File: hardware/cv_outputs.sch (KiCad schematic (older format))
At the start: 17 parts

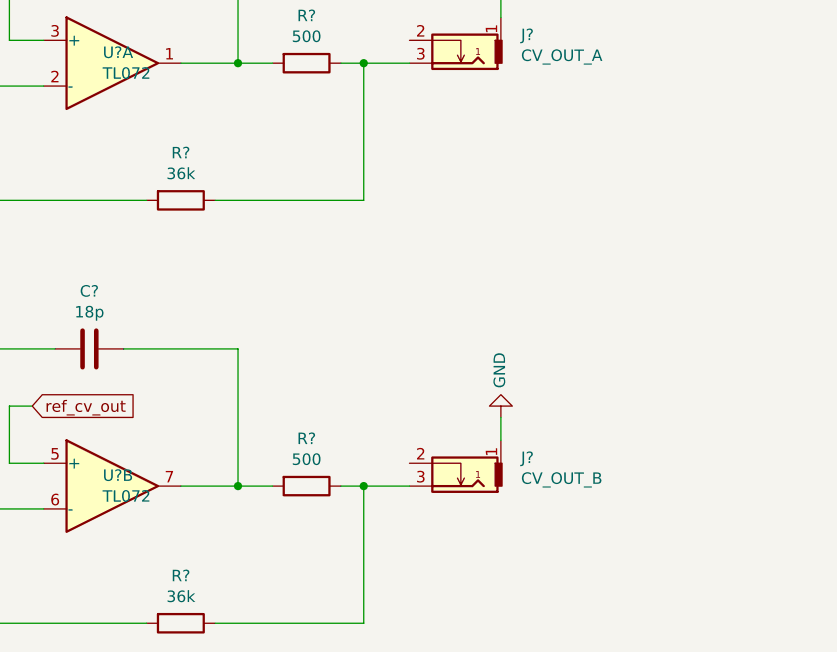
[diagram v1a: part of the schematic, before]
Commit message: Adjust CV-ins
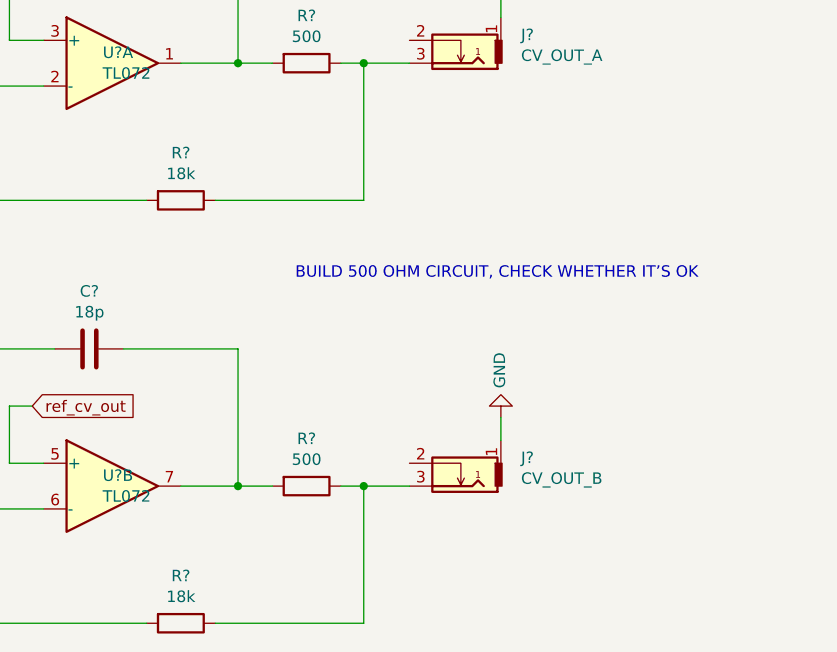
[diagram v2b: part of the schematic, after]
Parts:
- R? (x2): value 36k -> 18k
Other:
- note added: "BUILD 500 OHM CIRCUIT, CHECK WHETHER IT’S OK"
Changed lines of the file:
@@
 P 6900 3450
 F 0 "R?" V 6693 3450 50  0000 C CNN
-F 1 "36k" V 6784 3450 50  0000 C CNN
+F 1 "18k" V 6784 3450 50  0000 C CNN
 F 2 "" V 6830 3450 50  0001 C CNN
 F 3 "~" H 6900 3450 50  0001 C CNN
@@
 P 6900 5300
 F 0 "R?" V 6693 5300 50  0000 C CNN
-F 1 "36k" V 6784 5300 50  0000 C CNN
+F 1 "18k" V 6784 5300 50  0000 C CNN
 F 2 "" V 6830 5300 50  0001 C CNN
 F 3 "~" H 6900 5300 50  0001 C CNN
@@
 Wire Wire Line
 	7700 4700 7900 4700
+Text Notes 7400 3800 0    50   ~ 0
+BUILD 500 OHM CIRCUIT, CHECK WHETHER IT’S OK
 $EndSCHEMATC

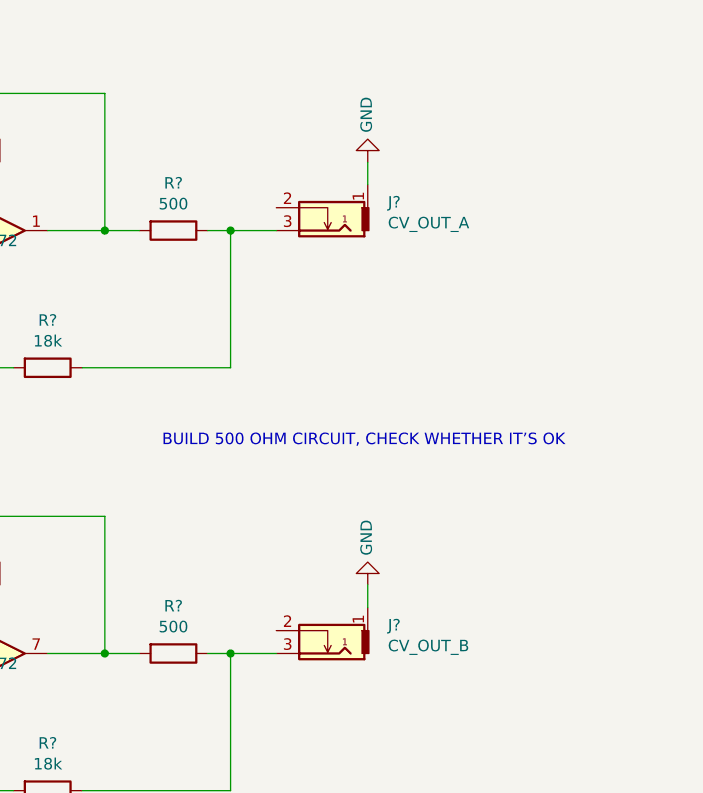
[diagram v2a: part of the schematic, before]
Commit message: Add more schematics:
- Faders
- Step LEDs
- Trigger output
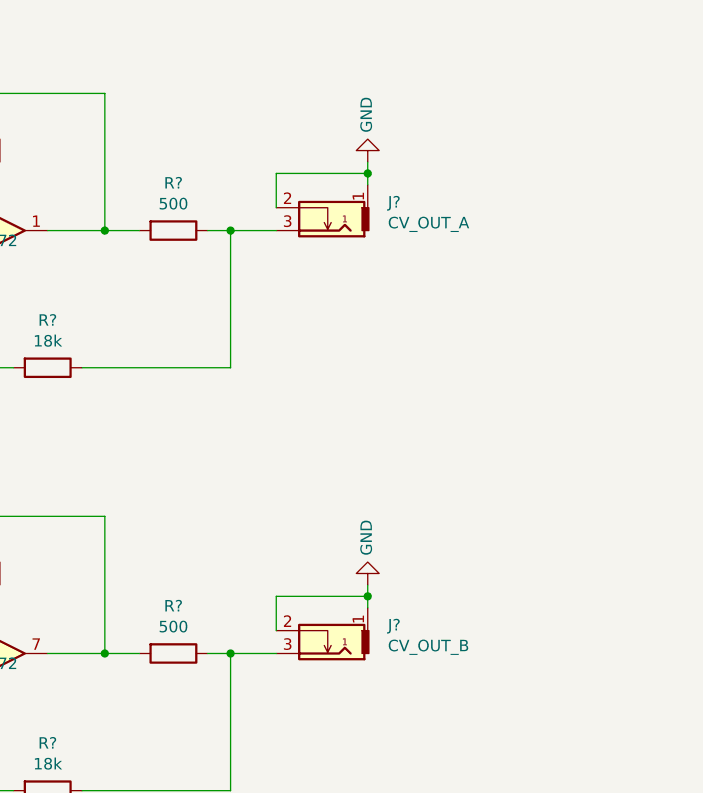
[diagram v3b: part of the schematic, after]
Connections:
- net GND: now also J?.2, J?.2
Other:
- note removed: "BUILD 500 OHM CIRCUIT, CHECK WHETHER IT’S OK"
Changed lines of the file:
@@
 $Descr A4 11693 8268
 encoding utf-8
-Sheet 4 6
+Sheet 4 9
 Title ""
 Date ""
@@
 $EndComp
 $Comp
-L power:GND #PWR?
+L power:GND #PWR0110
 U 1 1 5FB847AF
 P 1450 2000
-F 0 "#PWR?" H 1450 1750 50  0001 C CNN
+F 0 "#PWR0110" H 1450 1750 50  0001 C CNN
 F 1 "GND" V 1455 1872 50  0000 R CNN
 F 2 "" H 1450 2000 50  0001 C CNN
@@
 $EndComp
 $Comp
-L power:VEE #PWR?
+L power:VEE #PWR0111
 U 1 1 5FB9194E
 P 2650 2000
-F 0 "#PWR?" H 2650 1850 50  0001 C CNN
+F 0 "#PWR0111" H 2650 1850 50  0001 C CNN
 F 1 "VEE" H 2665 2173 50  0000 C CNN
 F 2 "" H 2650 2000 50  0001 C CNN
@@
 $EndComp
 $Comp
-L power:VCC #PWR?
+L power:VCC #PWR0112
 U 1 1 5FB924D1
 P 2650 1400
-F 0 "#PWR?" H 2650 1250 50  0001 C CNN
+F 0 "#PWR0112" H 2650 1250 50  0001 C CNN
 F 1 "VCC" H 2665 1573 50  0000 C CNN
 F 2 "" H 2650 1400 50  0001 C CNN
@@
 $EndComp
 $Comp
-L power:VCC #PWR?
+L power:VCC #PWR0113
 U 1 1 5FB9836B
 P 3650 1450
-F 0 "#PWR?" H 3650 1300 50  0001 C CNN
+F 0 "#PWR0113" H 3650 1300 50  0001 C CNN
 F 1 "VCC" H 3665 1623 50  0000 C CNN
 F 2 "" H 3650 1450 50  0001 C CNN
@@
 $EndComp
 $Comp
-L power:VEE #PWR?
+L power:VEE #PWR0114
 U 1 1 5FB98880
 P 4250 1450
-F 0 "#PWR?" H 4250 1300 50  0001 C CNN
+F 0 "#PWR0114" H 4250 1300 50  0001 C CNN
 F 1 "VEE" H 4265 1623 50  0000 C CNN
 F 2 "" H 4250 1450 50  0001 C CNN
@@
 $EndComp
 $Comp
-L power:GND #PWR?
+L power:GND #PWR0115
 U 1 1 5FB99275
 P 3950 1950
-F 0 "#PWR?" H 3950 1700 50  0001 C CNN
+F 0 "#PWR0115" H 3950 1700 50  0001 C CNN
 F 1 "GND" V 3955 1822 50  0000 R CNN
 F 2 "" H 3950 1950 50  0001 C CNN
@@
 $EndComp
 $Comp
-L power:GND #PWR?
+L power:GND #PWR0116
 U 1 1 5FBBFB43
 P 8300 2550
-F 0 "#PWR?" H 8300 2300 50  0001 C CNN
+F 0 "#PWR0116" H 8300 2300 50  0001 C CNN
 F 1 "GND" V 8305 2422 50  0000 R CNN
 F 2 "" H 8300 2550 50  0001 C CNN
@@
 $EndComp
 Wire Wire Line
-	8300 2550 8300 2650
+	8300 2550 8300 2600
 $Comp
 L thonkiconn_jackSocket_fuzzySi:fuzzySI_thonkiconn J?
@@
 $EndComp
 $Comp
-L power:GND #PWR?
+L power:GND #PWR0117
 U 1 1 5FBC5571
 P 8300 4400
-F 0 "#PWR?" H 8300 4150 50  0001 C CNN
+F 0 "#PWR0117" H 8300 4150 50  0001 C CNN
 F 1 "GND" V 8305 4272 50  0000 R CNN
 F 2 "" H 8300 4400 50  0001 C CNN
@@
 $EndComp
 Wire Wire Line
-	8300 4400 8300 4500
+	8300 4400 8300 4450
 Wire Wire Line
 	7700 2850 7900 2850
@@
 Wire Wire Line
 	7700 4700 7900 4700
-Text Notes 7400 3800 0    50   ~ 0
-BUILD 500 OHM CIRCUIT, CHECK WHETHER IT’S OK
+Wire Wire Line
+	7900 2750 7900 2600
+Wire Wire Line
+	7900 2600 8300 2600
+Connection ~ 8300 2600
+Wire Wire Line
+	8300 2600 8300 2650
+Wire Wire Line
+	7900 4600 7900 4450
+Wire Wire Line
+	7900 4450 8300 4450
+Connection ~ 8300 4450
+Wire Wire Line
+	8300 4450 8300 4500
 $EndSCHEMATC

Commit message: Minor adjustments to schematics before PCB
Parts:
- removed J?: CV_OUT_A, symbol thonkiconn_jackSocket_fuzzySi:fuzzySI_thonkiconn
- removed J?: CV_OUT_B, symbol thonkiconn_jackSocket_fuzzySi:fuzzySI_thonkiconn
- added J5, J6: PJ398SM, Connector_Audio:Jack_3.5mm_QingPu_WQP-PJ398SM_Vertical_CircularHoles, symbol Connector:AudioJack2_SwitchT
- C16, C17: renamed from C?; footprint (none) -> Capacitor_SMD:C_0603_1608Metric
- C18, C19: renamed from C?; value 18p -> 7p; footprint (none) -> Capacitor_SMD:C_0603_1608Metric
- R10, R11: renamed from R?; value 18k -> 270k; footprint (none) -> Resistor_SMD:R_0603_1608Metric
- R12, R13, R6, R7: renamed from R?; footprint (none) -> Resistor_SMD:R_0603_1608Metric
- R8, R9: renamed from R?; value 10k -> 75k; footprint (none) -> Resistor_SMD:R_0603_1608Metric
- U2: renamed from U?; footprint (none) -> Package_SO:SOIC-8_3.9x4.9mm_P1.27mm
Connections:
- net GND: now also J5.S, J5.TN, J6.S, J6.TN
- net at R11.1, R13.1: now also J6.T
- net at R10.1, R12.1: now also J5.T

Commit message: Last adjustments to hardware before v0.1 release
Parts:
- C17: renamed from C16; LCSC (none) -> C14663; LCSC Part # (none) -> C14663
- C18: renamed from C17; LCSC (none) -> C14663; LCSC Part # (none) -> C14663
- C19: renamed from C18; value 7p -> 10p; LCSC (none) -> C1634; LCSC Part # (none) -> C1634
- C20: renamed from C19; value 7p -> 10p; LCSC (none) -> C1634; LCSC Part # (none) -> C1634
- R12, R13: value 500 -> 470R; LCSC (none) -> C23179; LCSC Part # (none) -> C23179
- U2: LCSC (none) -> C6961; LCSC Part # (none) -> C6961
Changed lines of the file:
@@
 $EndComp
 $Comp
-L power:GND #PWR035
+L power:GND #PWR041
 U 1 1 5FB847AF
 P 1450 2000
-F 0 "#PWR035" H 1450 1750 50  0001 C CNN
+F 0 "#PWR041" H 1450 1750 50  0001 C CNN
 F 1 "GND" V 1455 1872 50  0000 R CNN
 F 2 "" H 1450 2000 50  0001 C CNN
@@
 F 6 "Y" H 6600 2850 50  0001 C CNN "Spice_Netlist_Enabled"
 F 7 "tl072-dual.cir" H 6600 2850 50  0001 C CNN "Spice_Lib_File"
+F 8 "C6961" H 6600 2850 50  0001 C CNN "LCSC Part #"
+F 9 "C6961" H 6600 2850 50  0001 C CNN "LCSC"
 	1    6600 2850
 	1    0    0    -1
 $EndComp
 $Comp
-L Device:C C18
+L Device:C C19
 U 1 1 5FB847D0
 P 6500 2250
-F 0 "C18" V 6248 2250 50  0000 C CNN
-F 1 "7p" V 6339 2250 50  0000 C CNN
+F 0 "C19" V 6248 2250 50  0000 C CNN
+F 1 "10p" V 6339 2250 50  0000 C CNN
 F 2 "Capacitor_SMD:C_0603_1608Metric" H 6538 2100 50  0001 C CNN
 F 3 "~" H 6500 2250 50  0001 C CNN
+F 4 "C1634" H 6500 2250 50  0001 C CNN "LCSC Part #"
+F 5 "C1634" H 6500 2250 50  0001 C CNN "LCSC"
 	1    6500 2250
 	0    1    1    0
@@
 P 7450 2850
 F 0 "R12" V 7243 2850 50  0000 C CNN
-F 1 "500" V 7334 2850 50  0000 C CNN
+F 1 "470R" V 7334 2850 50  0000 C CNN
 F 2 "Resistor_SMD:R_0603_1608Metric" V 7380 2850 50  0001 C CNN
 F 3 "~" H 7450 2850 50  0001 C CNN
+F 4 "C23179" H 7450 2850 50  0001 C CNN "LCSC Part #"
+F 5 "C23179" H 7450 2850 50  0001 C CNN "LCSC"
 	1    7450 2850
 	0    1    1    0
@@
 F 6 "Y" H 2750 1700 50  0001 C CNN "Spice_Netlist_Enabled"
 F 7 "tl072-dual.cir" H 2750 1700 50  0001 C CNN "Spice_Lib_File"
+F 8 "C6961" H 2750 1700 50  0001 C CNN "LCSC Part #"
+F 9 "C6961" H 2750 1700 50  0001 C CNN "LCSC"
 	3    2750 1700
 	1    0    0    -1
 $EndComp
 $Comp
-L power:VEE #PWR037
+L power:VEE #PWR043
 U 1 1 5FB9194E
 P 2650 2000
-F 0 "#PWR037" H 2650 1850 50  0001 C CNN
+F 0 "#PWR043" H 2650 1850 50  0001 C CNN
 F 1 "VEE" H 2665 2173 50  0000 C CNN
 F 2 "" H 2650 2000 50  0001 C CNN
@@
 $EndComp
 $Comp
-L power:VCC #PWR036
+L power:VCC #PWR042
 U 1 1 5FB924D1
 P 2650 1400
-F 0 "#PWR036" H 2650 1250 50  0001 C CNN
+F 0 "#PWR042" H 2650 1250 50  0001 C CNN
 F 1 "VCC" H 2665 1573 50  0000 C CNN
 F 2 "" H 2650 1400 50  0001 C CNN
@@
 F 6 "Y" H 6600 4700 50  0001 C CNN "Spice_Netlist_Enabled"
 F 7 "tl072-dual.cir" H 6600 4700 50  0001 C CNN "Spice_Lib_File"
+F 8 "C6961" H 6600 4700 50  0001 C CNN "LCSC Part #"
+F 9 "C6961" H 6600 4700 50  0001 C CNN "LCSC"
 	2    6600 4700
 	1    0    0    -1
 $EndComp
 $Comp
-L Device:C C19
+L Device:C C20
 U 1 1 5FB82D0C
 P 6500 4100
-F 0 "C19" V 6248 4100 50  0000 C CNN
-F 1 "7p" V 6339 4100 50  0000 C CNN
+F 0 "C20" V 6248 4100 50  0000 C CNN
+F 1 "10p" V 6339 4100 50  0000 C CNN
 F 2 "Capacitor_SMD:C_0603_1608Metric" H 6538 3950 50  0001 C CNN
 F 3 "~" H 6500 4100 50  0001 C CNN
+F 4 "C1634" H 6500 4100 50  0001 C CNN "LCSC Part #"
+F 5 "C1634" H 6500 4100 50  0001 C CNN "LCSC"
 	1    6500 4100
 	0    1    1    0
@@
 P 7450 4700
 F 0 "R13" V 7243 4700 50  0000 C CNN
-F 1 "500" V 7334 4700 50  0000 C CNN
+F 1 "470R" V 7334 4700 50  0000 C CNN
 F 2 "Resistor_SMD:R_0603_1608Metric" V 7380 4700 50  0001 C CNN
 F 3 "~" H 7450 4700 50  0001 C CNN
+F 4 "C23179" H 7450 4700 50  0001 C CNN "LCSC Part #"
+F 5 "C23179" H 7450 4700 50  0001 C CNN "LCSC"
 	1    7450 4700
 	0    1    1    0
@@
 dac_channel_b
 $Comp
-L Device:C C16
+L Device:C C17
 U 1 1 5FB976CE
 P 3650 1600
-F 0 "C16" V 3398 1600 50  0000 C CNN
+F 0 "C17" V 3398 1600 50  0000 C CNN
 F 1 "100n" V 3489 1600 50  0000 C CNN
 F 2 "Capacitor_SMD:C_0603_1608Metric" H 3688 1450 50  0001 C CNN
 F 3 "~" H 3650 1600 50  0001 C CNN
+F 4 "C14663" H 3650 1600 50  0001 C CNN "LCSC Part #"
+F 5 "C14663" H 3650 1600 50  0001 C CNN "LCSC"
 	1    3650 1600
 	-1   0    0    1
 $EndComp
 $Comp
-L Device:C C17
+L Device:C C18
 U 1 1 5FB97D49
 P 4250 1600
-F 0 "C17" V 3998 1600 50  0000 C CNN
+F 0 "C18" V 3998 1600 50  0000 C CNN
 F 1 "100n" V 4089 1600 50  0000 C CNN
 F 2 "Capacitor_SMD:C_0603_1608Metric" H 4288 1450 50  0001 C CNN
 F 3 "~" H 4250 1600 50  0001 C CNN
+F 4 "C14663" H 4250 1600 50  0001 C CNN "LCSC Part #"
+F 5 "C14663" H 4250 1600 50  0001 C CNN "LCSC"
 	1    4250 1600
 	-1   0    0    1
 $EndComp
 $Comp
-L power:VCC #PWR038
+L power:VCC #PWR044
 U 1 1 5FB9836B
 P 3650 1450
-F 0 "#PWR038" H 3650 1300 50  0001 C CNN
+F 0 "#PWR044" H 3650 1300 50  0001 C CNN
 F 1 "VCC" H 3665 1623 50  0000 C CNN
 F 2 "" H 3650 1450 50  0001 C CNN
@@
 $EndComp
 $Comp
-L power:VEE #PWR040
+L power:VEE #PWR046
 U 1 1 5FB98880
 P 4250 1450
-F 0 "#PWR040" H 4250 1300 50  0001 C CNN
+F 0 "#PWR046" H 4250 1300 50  0001 C CNN
 F 1 "VEE" H 4265 1623 50  0000 C CNN
 F 2 "" H 4250 1450 50  0001 C CNN
@@
 $EndComp
 $Comp
-L power:GND #PWR039
+L power:GND #PWR045
 U 1 1 5FB99275
 P 3950 1950
-F 0 "#PWR039" H 3950 1700 50  0001 C CNN
+F 0 "#PWR045" H 3950 1700 50  0001 C CNN
 F 1 "GND" V 3955 1822 50  0000 R CNN
 F 2 "" H 3950 1950 50  0001 C CNN
@@
 	8100 2950 8100 3000
 $Comp
-L power:GND #PWR041
+L power:GND #PWR047
 U 1 1 5FBBFB43
 P 8100 3100
-F 0 "#PWR041" H 8100 2850 50  0001 C CNN
+F 0 "#PWR047" H 8100 2850 50  0001 C CNN
 F 1 "GND" V 8105 2972 50  0000 R CNN
 F 2 "" H 8100 3100 50  0001 C CNN
@@
 	8100 4800 8100 4850
 $Comp
-L power:GND #PWR042
+L power:GND #PWR048
 U 1 1 5FEFC60D
 P 8100 4950
-F 0 "#PWR042" H 8100 4700 50  0001 C CNN
+F 0 "#PWR048" H 8100 4700 50  0001 C CNN
 F 1 "GND" V 8105 4822 50  0000 R CNN
 F 2 "" H 8100 4950 50  0001 C CNN

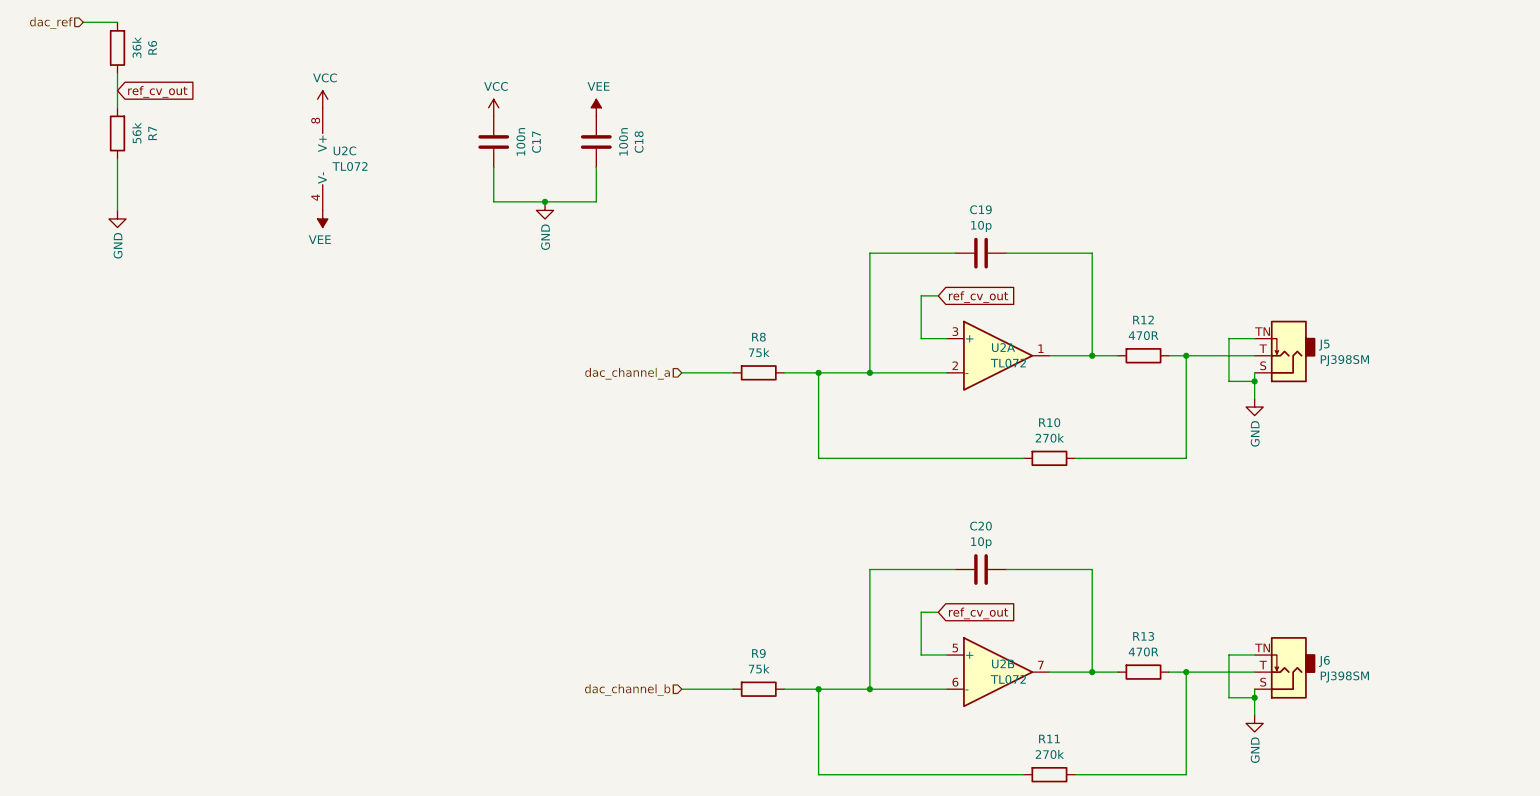
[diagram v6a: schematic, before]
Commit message: Re-adjust resistor values for CV-out
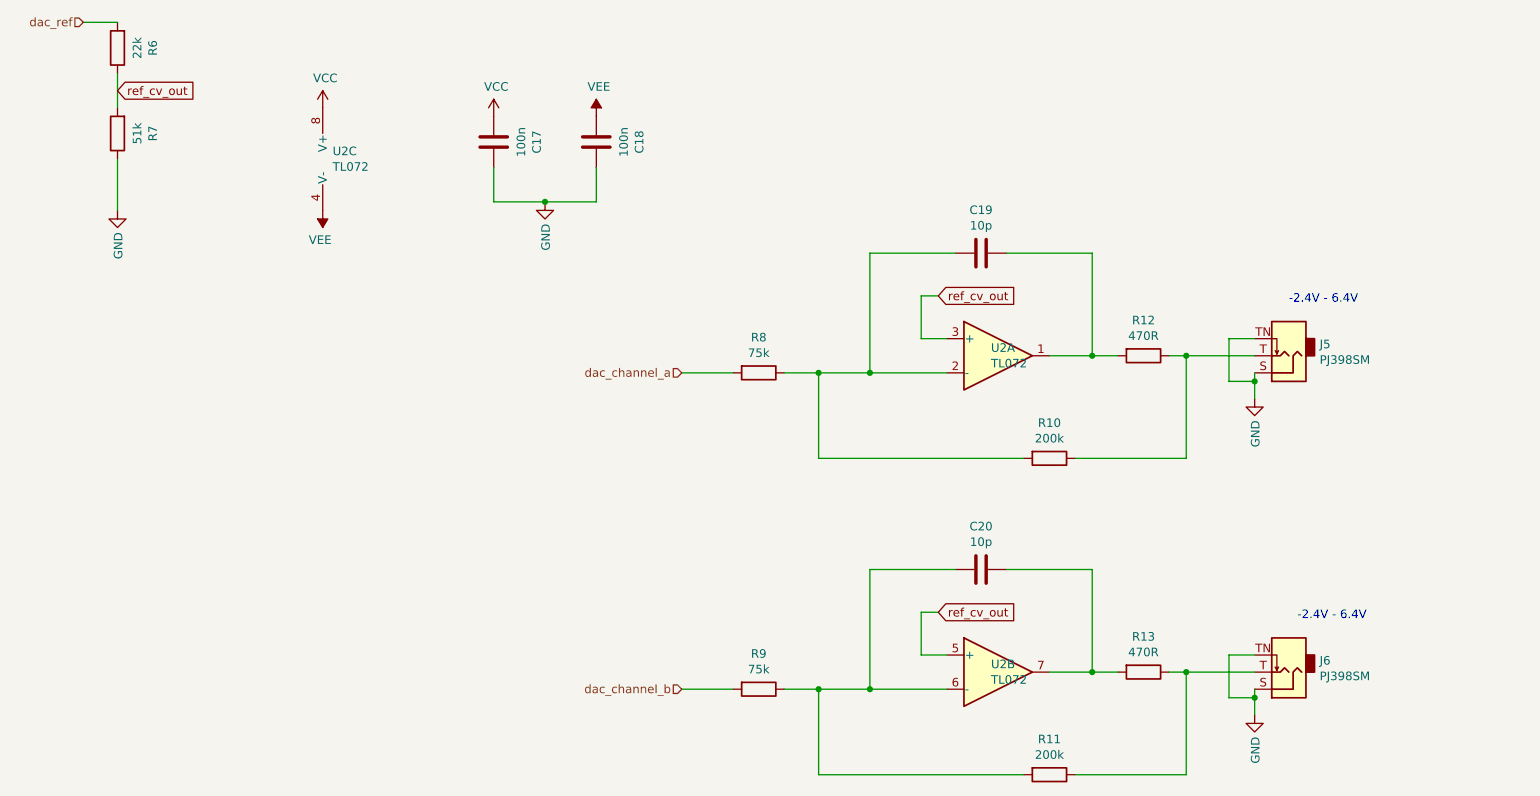
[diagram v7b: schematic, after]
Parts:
- R10, R11: value 270k -> 200k
- R6: value 36k -> 22k
- R7: value 56k -> 51k
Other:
- note added: "-2.4V - 6.4V"
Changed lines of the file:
@@
 P 1450 1050
 F 0 "R6" V 1243 1050 50  0000 C CNN
-F 1 "36k" V 1334 1050 50  0000 C CNN
+F 1 "22k" V 1334 1050 50  0000 C CNN
 F 2 "Resistor_SMD:R_0603_1608Metric" V 1380 1050 50  0001 C CNN
 F 3 "~" H 1450 1050 50  0001 C CNN
@@
 P 1450 1550
 F 0 "R7" V 1243 1550 50  0000 C CNN
-F 1 "56k" V 1334 1550 50  0000 C CNN
+F 1 "51k" V 1334 1550 50  0000 C CNN
 F 2 "Resistor_SMD:R_0603_1608Metric" V 1380 1550 50  0001 C CNN
 F 3 "~" H 1450 1550 50  0001 C CNN
@@
 P 6900 3450
 F 0 "R10" V 6693 3450 50  0000 C CNN
-F 1 "270k" V 6784 3450 50  0000 C CNN
+F 1 "200k" V 6784 3450 50  0000 C CNN
 F 2 "Resistor_SMD:R_0603_1608Metric" V 6830 3450 50  0001 C CNN
 F 3 "~" H 6900 3450 50  0001 C CNN
@@
 P 6900 5300
 F 0 "R11" V 6693 5300 50  0000 C CNN
-F 1 "270k" V 6784 5300 50  0000 C CNN
+F 1 "200k" V 6784 5300 50  0000 C CNN
 F 2 "Resistor_SMD:R_0603_1608Metric" V 6830 5300 50  0001 C CNN
 F 3 "~" H 6900 5300 50  0001 C CNN
@@
 	8100 4850 8100 4950
 Connection ~ 7700 4700
+Text Notes 8300 2550 0    50   ~ 0
+-2.4V - 6.4V
+Text Notes 8350 4400 0    50   ~ 0
+-2.4V - 6.4V
 $EndSCHEMATC
